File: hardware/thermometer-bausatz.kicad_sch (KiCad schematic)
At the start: 34 parts, among them J1 TEST_1P, J2 TEST_1P, J3 ISP, U1 ATTINY24A-SSU, U2 MCP9700AT-E_TT

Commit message: Resolve DRC errors
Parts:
- C1, C2: footprint Capacitors_SMD:C_0805_HandSoldering -> Capacitor_SMD:C_0805_2012Metric_Pad1.18x1.45mm_HandSolder
- D1, D10, D11, D2, D3, D4, D5, D6, D7, D8, D9: footprint LEDs:LED-3MM -> LED_THT:LED_D3.0mm
- J1, J2: footprint Wire_Pads:SolderWirePad_single_1-5mmDrill -> TestPoint:TestPoint_THTPad_D3.0mm_Drill1.5mm
- J3: footprint Pin_Headers:Pin_Header_Straight_2x03 -> Connector_PinHeader_2.54mm:PinHeader_2x03_P2.54mm_Vertical
- R1: footprint Resistors_SMD:R_0805_HandSoldering -> Resistor_SMD:R_0805_2012Metric_Pad1.20x1.40mm_HandSolder
- U1: footprint Housings_SOIC:SOIC-14_3.9x8.7mm_Pitch1.27mm -> Package_SO:SOIC-14_3.9x8.7mm_P1.27mm
- U2: footprint TO_SOT_Packages_SMD:SOT-23 -> Package_TO_SOT_SMD:SOT-23
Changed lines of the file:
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@@
       (effects (font (size 1.27 1.27)))
     )
-    (property "Footprint" "Housings_SOIC:SOIC-14_3.9x8.7mm_Pitch1.27mm" (at 95.25 107.95 0)
+    (property "Footprint" "Package_SO:SOIC-14_3.9x8.7mm_P1.27mm" (at 95.25 107.95 0)
       (effects (font (size 1.27 1.27) italic) hide)
     )
@@
       (effects (font (size 1.27 1.27)) (justify left))
     )
-    (property "Footprint" "Capacitors_SMD:C_0805_HandSoldering" (at 64.4652 106.68 0)
+    (property "Footprint" "Capacitor_SMD:C_0805_2012Metric_Pad1.18x1.45mm_HandSolder" (at 64.4652 106.68 0)
       (effects (font (size 1.27 1.27)) hide)
     )
@@
       (effects (font (size 1.27 1.27)))
     )
-    (property "Footprint" "Wire_Pads:SolderWirePad_single_1-5mmDrill" (at 59.69 82.55 0)
+    (property "Footprint" "TestPoint:TestPoint_THTPad_D3.0mm_Drill1.5mm" (at 59.69 82.55 0)
       (effects (font (size 1.27 1.27)) hide)
     )
@@
       (effects (font (size 1.27 1.27)))
     )
-    (property "Footprint" "Wire_Pads:SolderWirePad_single_1-5mmDrill" (at 59.69 113.03 0)
+    (property "Footprint" "TestPoint:TestPoint_THTPad_D3.0mm_Drill1.5mm" (at 59.69 113.03 0)
       (effects (font (size 1.27 1.27)) hide)
     )
@@
       (effects (font (size 1.27 1.27)))
     )
-    (property "Footprint" "Pin_Headers:Pin_Header_Straight_2x03" (at 153.67 102.87 0)
+    (property "Footprint" "Connector_PinHeader_2.54mm:PinHeader_2x03_P2.54mm_Vertical" (at 153.67 102.87 0)
       (effects (font (size 1.27 1.27)) hide)
     )
@@
       (effects (font (size 1.27 1.27)))
     )
-    (property "Footprint" "LEDs:LED-3MM" (at 139.7 74.93 0)
+    (property "Footprint" "LED_THT:LED_D3.0mm" (at 139.7 74.93 0)
       (effects (font (size 1.27 1.27)) hide)
     )
@@
       (effects (font (size 1.27 1.27)))
     )
-    (property "Footprint" "LEDs:LED-3MM" (at 147.32 74.93 0)
+    (property "Footprint" "LED_THT:LED_D3.0mm" (at 147.32 74.93 0)
       (effects (font (size 1.27 1.27)) hide)
     )
@@
       (effects (font (size 1.27 1.27)))
     )
-    (property "Footprint" "LEDs:LED-3MM" (at 154.94 74.93 0)
+    (property "Footprint" "LED_THT:LED_D3.0mm" (at 154.94 74.93 0)
       (effects (font (size 1.27 1.27)) hide)
     )
@@
       (effects (font (size 1.27 1.27)))
     )
-    (property "Footprint" "LEDs:LED-3MM" (at 162.56 74.93 0)
+    (property "Footprint" "LED_THT:LED_D3.0mm" (at 162.56 74.93 0)
       (effects (font (size 1.27 1.27)) hide)
     )
@@
       (effects (font (size 1.27 1.27)))
     )
-    (property "Footprint" "LEDs:LED-3MM" (at 170.18 74.93 0)
+    (property "Footprint" "LED_THT:LED_D3.0mm" (at 170.18 74.93 0)
       (effects (font (size 1.27 1.27)) hide)
     )
@@
       (effects (font (size 1.27 1.27)))
     )
-    (property "Footprint" "LEDs:LED-3MM" (at 177.8 74.93 0)
+    (property "Footprint" "LED_THT:LED_D3.0mm" (at 177.8 74.93 0)
       (effects (font (size 1.27 1.27)) hide)
     )
@@
       (effects (font (size 1.27 1.27)))
     )
-    (property "Footprint" "LEDs:LED-3MM" (at 185.42 74.93 0)
+    (property "Footprint" "LED_THT:LED_D3.0mm" (at 185.42 74.93 0)
       (effects (font (size 1.27 1.27)) hide)
     )
@@
       (effects (font (size 1.27 1.27)))
     )
-    (property "Footprint" "LEDs:LED-3MM" (at 193.04 74.93 0)
+    (property "Footprint" "LED_THT:LED_D3.0mm" (at 193.04 74.93 0)
       (effects (font (size 1.27 1.27)) hide)
     )
@@
       (effects (font (size 1.27 1.27)))
     )
-    (property "Footprint" "LEDs:LED-3MM" (at 200.66 74.93 0)
+    (property "Footprint" "LED_THT:LED_D3.0mm" (at 200.66 74.93 0)
       (effects (font (size 1.27 1.27)) hide)
     )
@@
       (effects (font (size 1.27 1.27)))
     )
-    (property "Footprint" "LEDs:LED-3MM" (at 208.28 74.93 0)
+    (property "Footprint" "LED_THT:LED_D3.0mm" (at 208.28 74.93 0)
       (effects (font (size 1.27 1.27)) hide)
     )
@@
       (effects (font (size 1.27 1.27)))
     )
-    (property "Footprint" "LEDs:LED-3MM" (at 215.9 74.93 0)
+    (property "Footprint" "LED_THT:LED_D3.0mm" (at 215.9 74.93 0)
       (effects (font (size 1.27 1.27)) hide)
     )
@@
       (effects (font (size 1.27 1.27)) (justify right))
     )
-    (property "Footprint" "TO_SOT_Packages_SMD:SOT-23" (at 85.09 63.5 0)
+    (property "Footprint" "Package_TO_SOT_SMD:SOT-23" (at 85.09 63.5 0)
       (effects (font (size 1.27 1.27)) hide)
     )
@@
       (effects (font (size 1.27 1.27)) (justify left))
     )
-    (property "Footprint" "Resistors_SMD:R_0805_HandSoldering" (at 109.22 55.118 90)
+    (property "Footprint" "Resistor_SMD:R_0805_2012Metric_Pad1.20x1.40mm_HandSolder" (at 109.22 55.118 90)
       (effects (font (size 1.27 1.27)) hide)
     )
@@
       (effects (font (size 1.27 1.27)) (justify left))
     )
-    (property "Footprint" "Capacitors_SMD:C_0805_HandSoldering" (at 56.8452 58.42 0)
-      (effects (font (size 1.27 1.27)) hide)
-    )
+    (property "Footprint" "Capacitor_SMD:C_0805_2012Metric_Pad1.18x1.45mm_HandSolder" (at 56.8452 58.42 0)
+      (effects (font (size 1.27 1.27)) hide)
+    )

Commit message: Modernize everything
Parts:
- added B2: ~, Thermometer-Bausatz:bastelecke-url, symbol misc:Image
- B1: symbol battery_holder:battery_holder -> misc:battery_holder
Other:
- note added: "QR-Code https://www.darc.de/der-club/distrikte/s/ortsverbaende/09/bastelecke-des-ov-s09/"
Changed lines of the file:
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@@
     )
+  )
+  (text "QR-Code\nhttps://www.darc.de/der-club/distrikte/s/ortsverbaende/09/bastelecke-des-ov-s09/"
+    (at 43.18 165.1 0)
+    (effects (font (size 1.27 1.27)) (justify left bottom))
   )
   (text "Vcc\nMOSI\nGND" (at 172.72 106.68 0)
@@
     )
   )
-  (symbol (lib_id "battery_holder:battery_holder") (at 76.2 143.51 0) (unit 1)
+  (symbol (lib_id "misc:battery_holder") (at 76.2 143.51 0) (unit 1)
     (in_bom yes) (on_board yes) (dnp no)
     (property "Reference" "B1" (at 76.2 143.51 0)
@@
         )
       )
+    )
+  )
+  (symbol (lib_id "misc:Image") (at 76.2 157.48 0) (unit 1)
+    (in_bom yes) (on_board yes) (dnp no) (fields_autoplaced)
+    (property "Reference" "B2" (at 80.645 157.7968 0)
+      (effects (font (size 1.27 1.27)) (justify left))
+    )
+    (property "Value" "~" (at 76.2 157.48 0)
+      (effects (font (size 1.27 1.27)))
+    )
+    (property "Footprint" "Thermometer-Bausatz:bastelecke-url" (at 76.2 157.48 0)
+      (effects (font (size 1.27 1.27)) hide)
+    )
+    (property "Datasheet" "" (at 76.2 157.48 0)
+      (effects (font (size 1.27 1.27)) hide)
+    )
+    (instances
+      (project "thermometer-bausatz"
+        (path "/b629b0f3-9b5f-44da-8346-e958d88e091c"
+          (reference "B2") (unit 1)
+        )
+      )

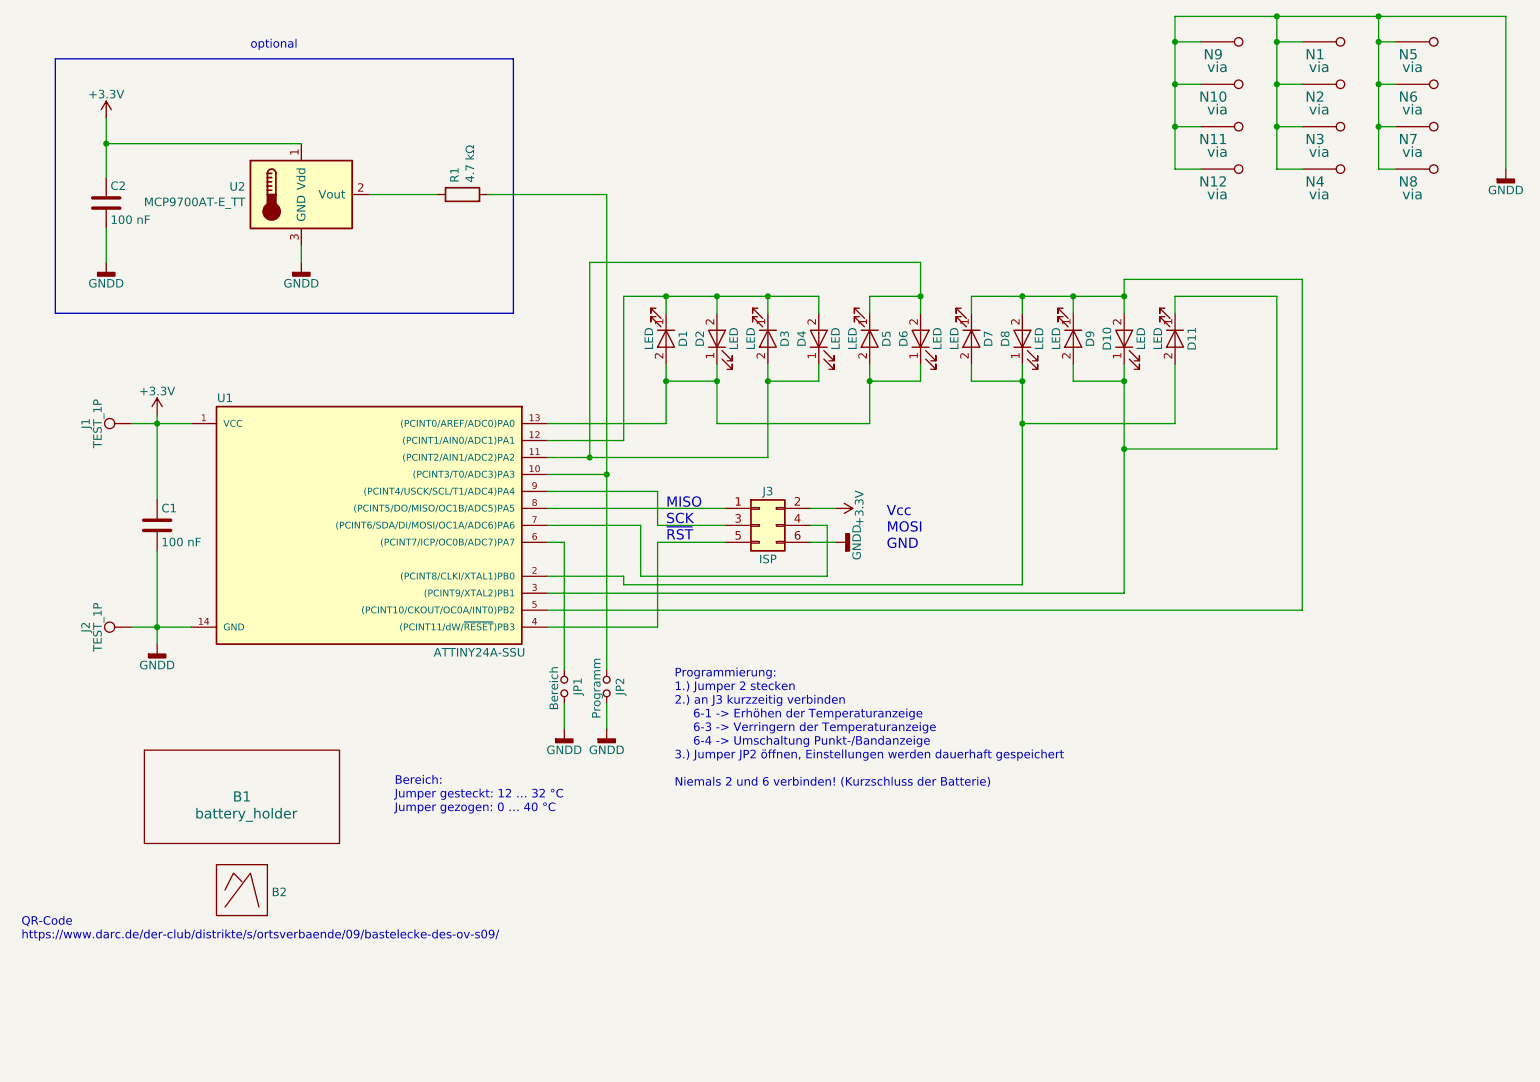
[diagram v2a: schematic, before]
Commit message: Replace ATtiny24 by AVR16EB14
While both controllers share the same footprint, the AVR16EB14
is quite a bit different. To begin, the footprints have VDD and
GND swapped. The AVRxEB uses UPDI for programming, so basically
only a single wire is needed. The GPIOs are scattered across
more ports. Finally, the entire clock system and ADC is
different.
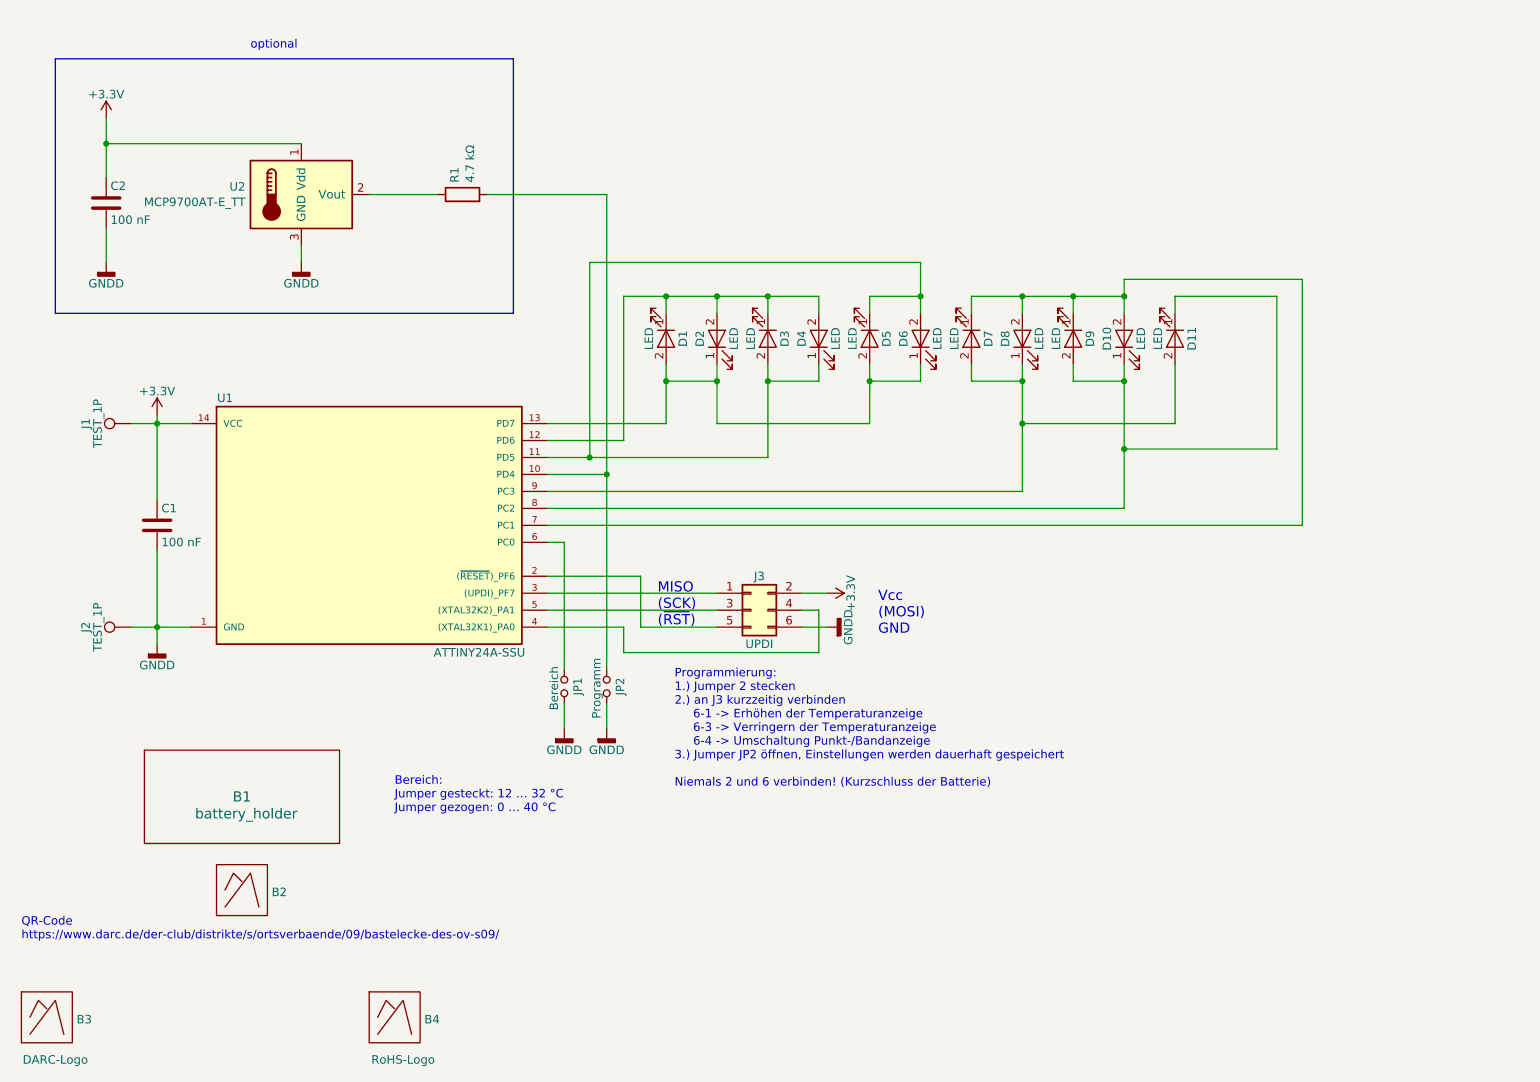
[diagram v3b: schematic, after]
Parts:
- removed N1, N10, N11, N12, N2, N3, N4, N5, N6, N7, N8, N9: via, Thermometer-Bausatz:via-0.3-0.6, symbol thermometer-bausatz-rescue:via
- added B3: DARC-Logo, Thermometer-Bausatz:DARC-Raute, symbol misc:Image
- added B4: RoHS-Logo, Thermometer-Bausatz:RoHS_Silk, symbol misc:Image
- J3: value ISP -> UPDI
- U1: symbol thermometer-bausatz-rescue:ATTINY24A-SSU-atmel -> misc:AVRxEB14
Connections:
- net +3V3: now also U1.14 (VCC); no longer U1.1 (VCC)
- net GNDD: now also U1.1 (GND); no longer U1.14 (GND)
- net at D11.2 (A), D7.2 (A), D8.1 (K): now also U1.9 (PC3); no longer U1.2 ((PCINT8/CLKI/XTAL1)PB0)
- net at D10.1 (K), D11.1 (K), D9.2 (A): now also U1.8 (PC2); no longer U1.3 ((PCINT9/XTAL2)PB1)
- net at J3.5 (Pin_5): now also U1.2 ((~{RESET})_PF6); no longer U1.4 ((PCINT11/dW/~{RESET})PB3)
- net at D10.2 (A), D7.1 (K), D8.2 (A)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: now also U1.7 (PC1); no longer U1.5 ((PCINT10/CKOUT/OC0A/INT0)PB2)
- net at J3.4 (Pin_4): now also U1.4 ((XTAL32K1)_PA0); no longer U1.7 ((PCINT6/SDA/DI/MOSI/OC1A/ADC6)PA6)
- net at J3.1 (Pin_1): now also U1.3 ((UPDI)_PF7); no longer U1.8 ((PCINT5/DO/MISO/OC1B/ADC5)PA5)
- net at J3.3 (Pin_3): now also U1.5 ((XTAL32K2)_PA1); no longer U1.9 ((PCINT4/USCK/SCL/T1/ADC4)PA4)
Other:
- note added: "MISO (SCK) (~{RST})"
- note added: "Vcc (MOSI) GND"
- note removed: "MISO SCK ~{RST}"
- note removed: "Vcc MOSI GND"
- moved on the sheet: J3
